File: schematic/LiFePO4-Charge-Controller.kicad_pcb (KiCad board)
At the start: 2 copper layers, 51 parts

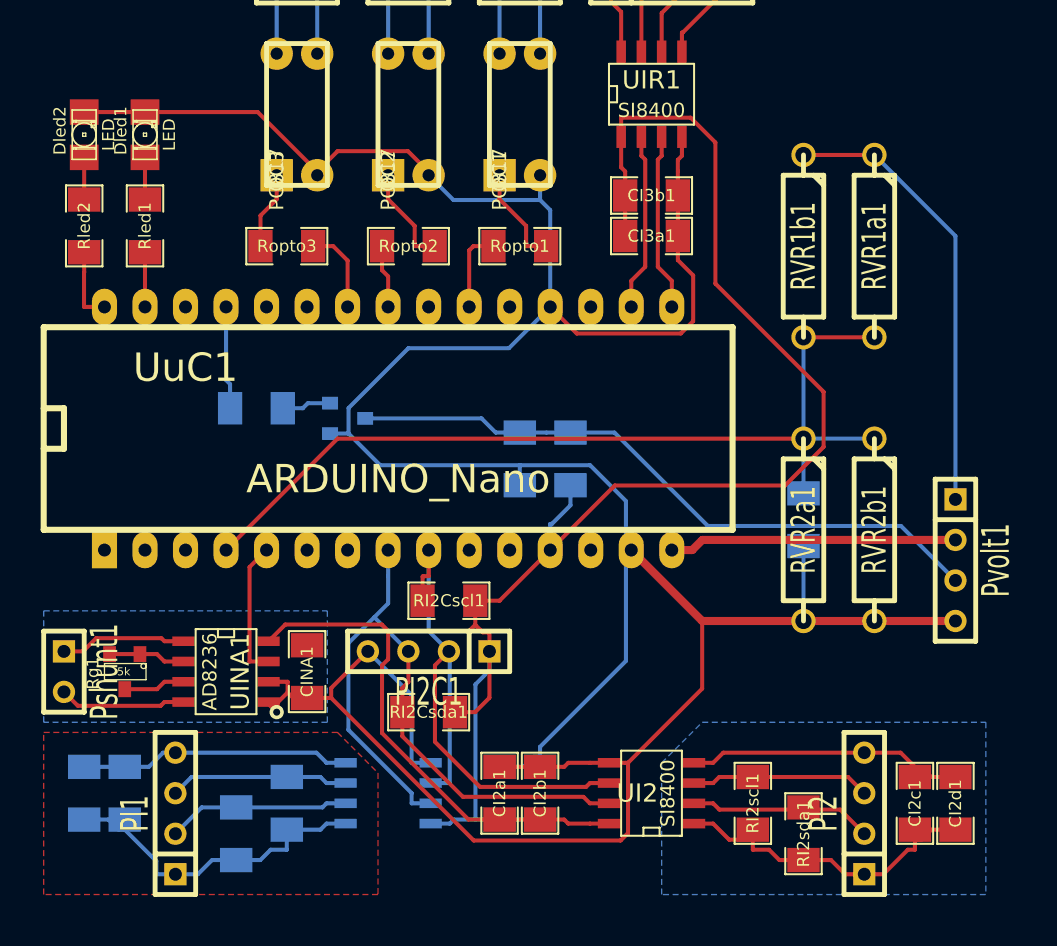
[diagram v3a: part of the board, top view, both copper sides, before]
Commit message: PWM/PID code corrected. PCB: In-Amp pad (module) corrected. Board done.
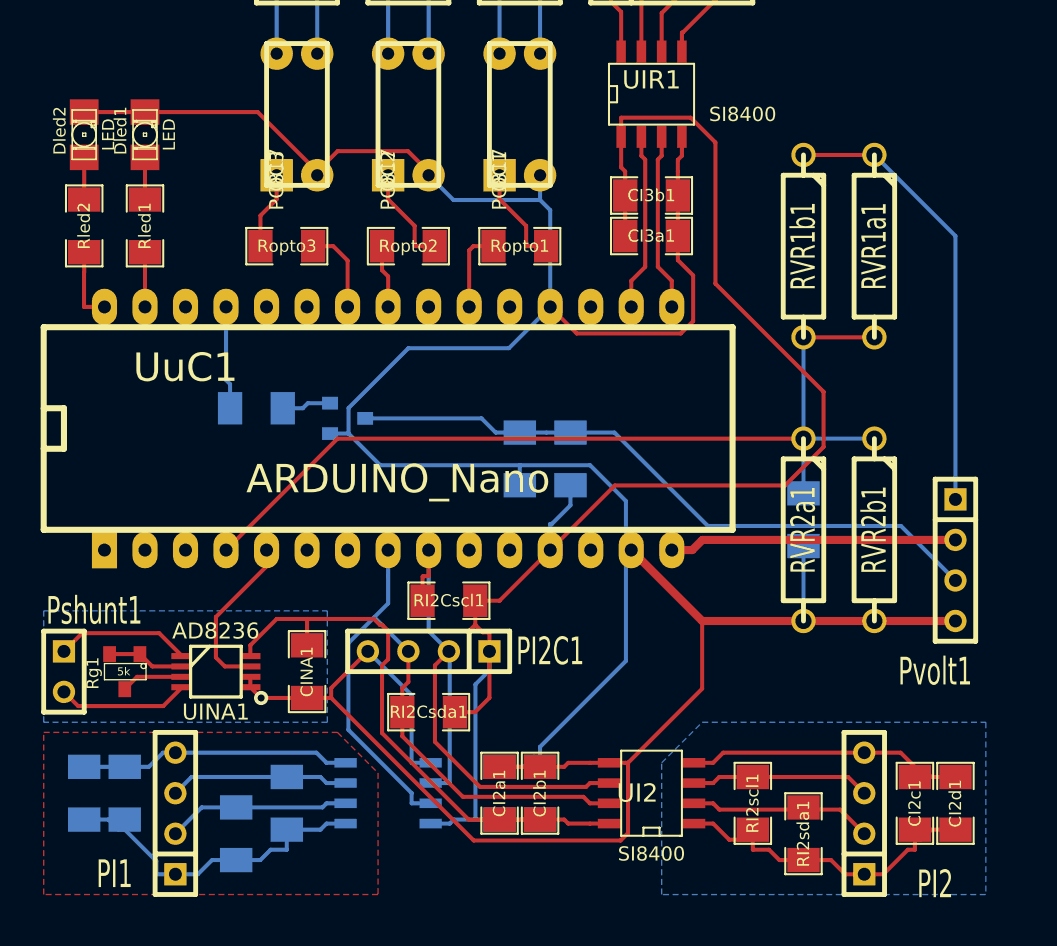
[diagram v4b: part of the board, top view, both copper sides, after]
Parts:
- UINA1: footprint SO8E -> MSOP_8
- moved UINA1 0.63 mm to (196.2, 152.4)
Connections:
- CINA1 pad 1: (no net) -> 5v
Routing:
- net 5v: track 130.4 -> 134.3 mm
- net N-0000034: track 8.62 -> 10.4 mm
- net Gnd: track 244.7 -> 243.7 mm
- net N-0000036: track 7.91 -> 8.46 mm
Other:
- net class Default: clearance 0.3675 -> 0.254
- rule trace_clearance: 0.3675 -> 0.254
